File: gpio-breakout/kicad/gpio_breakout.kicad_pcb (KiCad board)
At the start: 2 copper layers, 63.5 x 30 mm, 12 parts, among them J1 FH41-40S-0.5SH(05), J2 Pi GPIO 2x20

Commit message: gpio-breakout: attach FH41 STEP model, tidy silk
Real connector model from the shared B2_INTERCONNECT.3dshapes now
renders on J1; redundant 3V3/GND silk texts removed (TP refs + README
cover them).

Co-Authored-By: Claude Fable 5 <noreply@anthropic.com>
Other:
- board text removed: "3V3"
- board text removed: "GND"
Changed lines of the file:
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@@
 		)
 		(embedded_fonts no)
-		(model "${KIPRJMOD}/B2_INTERCONNECT.3dshapes/FPC-SMD_FH41-40S-0.5SH.step"
+		(model "${KIPRJMOD}/../B2_INTERCONNECT.3dshapes/FPC-SMD_FH41-40S-0.5SH.step"
 			(offset
 				(xyz 0 0 0)
@@
 		(layer "F.SilkS")
 		(effects
-			(font
-				(size 1 1)
-				(thickness 0.15)
-			)
-		)
-	)
-	(gr_text "3V3"
-		(at 108.2 72.6 0)
-		(layer "F.SilkS")
-		(effects
-			(font
-				(size 1 1)
-				(thickness 0.15)
-			)
-		)
-	)
-	(gr_text "GND"
-		(at 108.2 78 0)
-		(layer "F.SilkS")
-		(effects

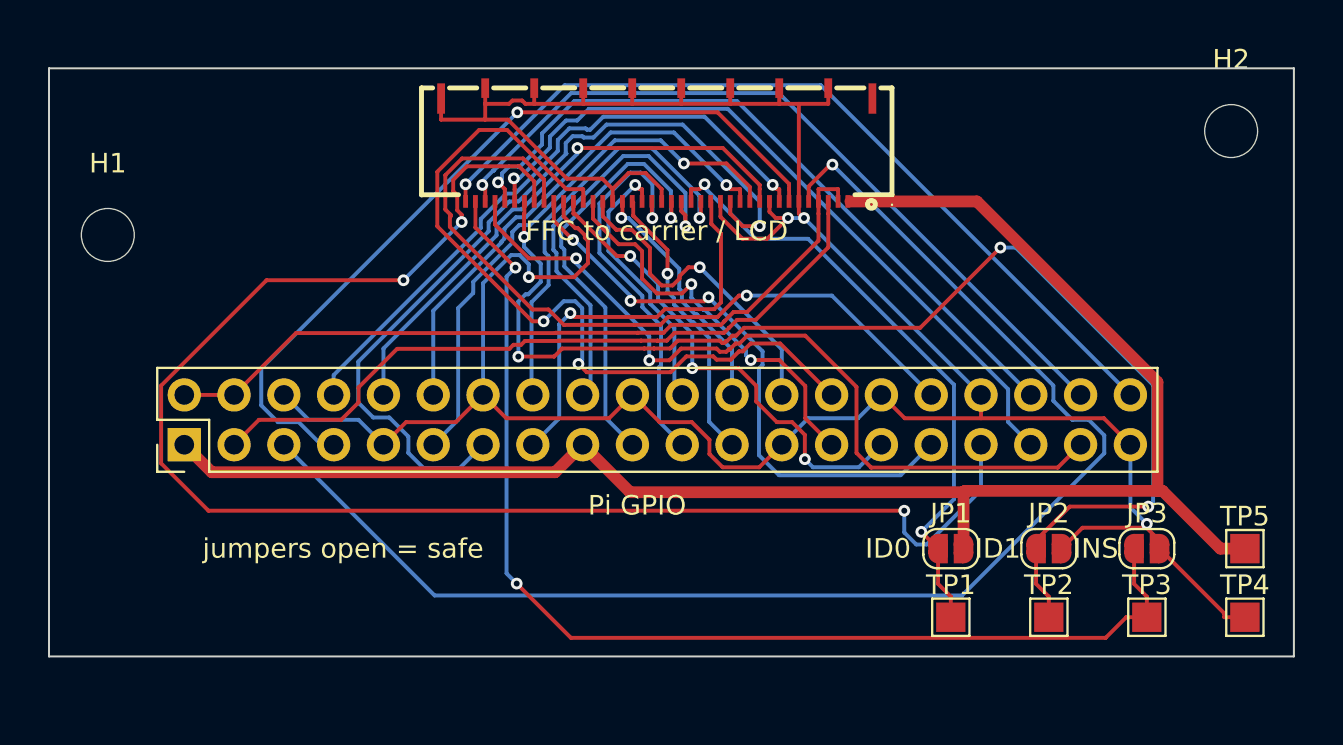
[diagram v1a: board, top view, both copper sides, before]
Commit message: gpio-breakout A1: address design review
4-layer with solid In1 GND plane + pours (review #2), corrected FH41
land pattern 0.30x0.65 with paste margin (#4), pads 41-50 shield to
GND (#4), fused + default-bridged/cuttable 5V/3V3 links (#3), symbol
pins retyped passive (#7), fresh all-severity ERC/DRC committed (#6,
#7), J2 assembly split defined (#9), honest gate statements in README
(#2, #8). Board grown to 63.5x32 for full routing: errors-only DRC
0/0/0, zero dangling copper. Fabrication remains gated on the
interconnect contract cable identity (#1, #5).

Co-Authored-By: Claude Fable 5 <noreply@anthropic.com>
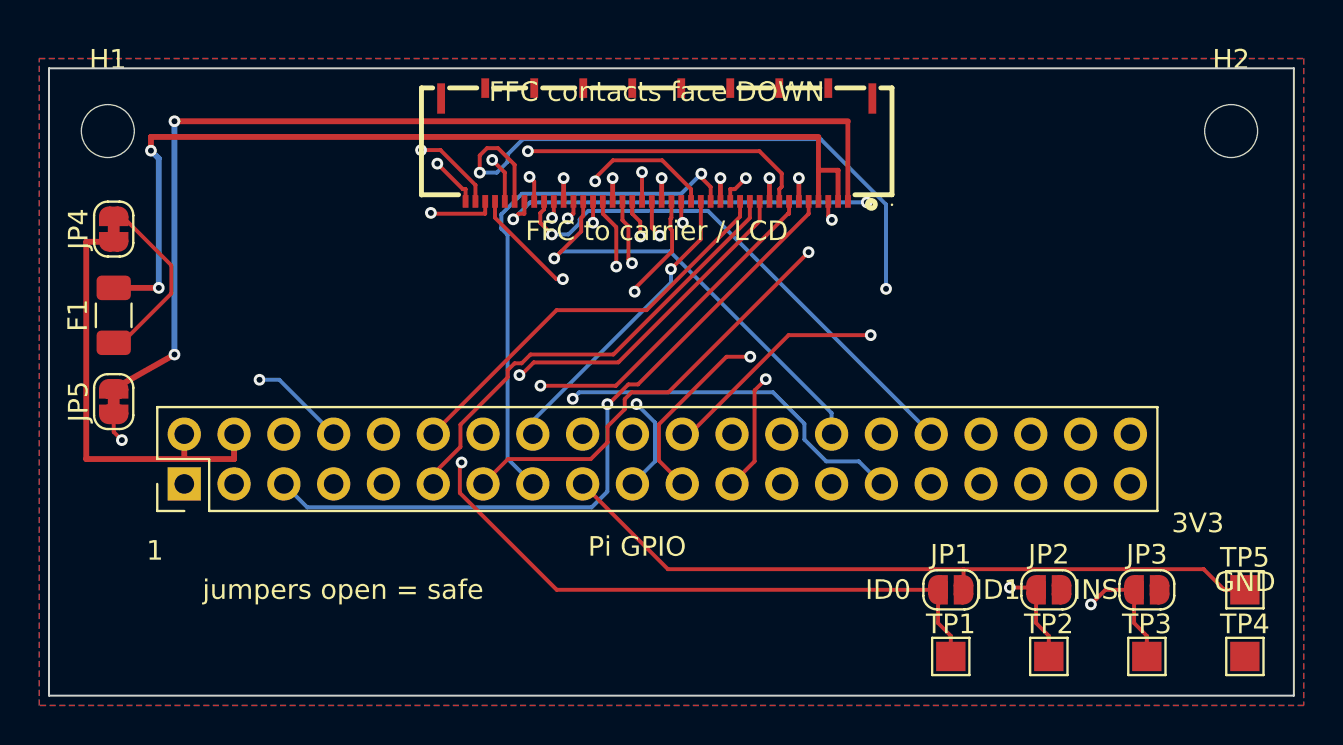
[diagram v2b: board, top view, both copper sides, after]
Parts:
- added F1: 0.5A polyfuse 1206, Fuse_1206_3216Metric, F.Cu at (53.3, 62.6)
- added JP4: 5V LINK, SolderJumper-2_P1.3mm_Bridged_RoundedPad1.0x1.5mm, F.Cu at (53.3, 58.2)
- added JP5: 3V3 LINK, SolderJumper-2_P1.3mm_Bridged_RoundedPad1.0x1.5mm, F.Cu at (53.3, 67.0)
- moved H1 5.30 mm to (53.0, 53.2)
- moved JP1 2.10 mm to (96.0, 76.6)
- moved JP2 2.10 mm to (101.0, 76.6)
- moved JP3 2.10 mm to (106.0, 76.6)
- moved TP5 2.10 mm to (111.0, 76.6)
- moved J2 2.00 mm to (56.9, 71.2)
- moved TP1 2.00 mm to (96.0, 80.0)
- moved TP2 2.00 mm to (101.0, 80.0)
- moved TP3 2.00 mm to (106.0, 80.0)
- moved TP4 2.00 mm to (111.0, 80.0)
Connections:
- J1 pad 1: +3V3 -> +3V3_FFC
- J1 pad 2: +5V -> +5V_FFC
- J1 pad 4: +5V -> +5V_FFC
- J1 pad 50: (no net) -> GND
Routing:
- net GND: track 152.0 -> 7.14 mm, vias 4 -> 6
- net +3V3_FFC: track 0.00 -> 53.9 mm, vias 0 -> 2
- net +5V_FFC: track 0.00 -> 50.1 mm, vias 0 -> 2
- net GPIO13: track 78.5 -> 36.3 mm, vias 3 -> 1
- net GPIO3: track 71.4 -> 36.7 mm
- net PANEL_ID0: track 31.7 -> 57.9 mm
- net +3V3: track 85.6 -> 64.2 mm, vias 0 -> 1
- net ID_SC: track 40.8 -> 22.3 mm, vias 2 -> 1
- net +5V: track 39.9 -> 22.6 mm
- net GPIO25: track 13.9 -> 31.1 mm, vias 1 -> 2
- net GPIO27: track 42.3 -> 29.0 mm, vias 1 -> 2
- net GPIO12: track 39.1 -> 26.7 mm
- net PANEL_ID1: track 63.5 -> 51.8 mm, vias 4 -> 3
- net GPIO4: track 41.2 -> 30.0 mm
- net +5V_LNK: track 0.00 -> 9.39 mm
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- added copper zone on B.Cu, net GND
- added copper zone on F.Cu, net GND
- added copper zone on In1.Cu, net GND
- added copper zone on In2.Cu, net GND
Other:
- board size 63.5 x 30 mm -> 63.5 x 32 mm
- copper layers 2 -> 4
- board text added: "1"
- board text added: "3V3"
- board text added: "FFC contacts face DOWN"
- board text added: "GND"
- board text added: "cut 5V/3V3 links if chain"
- board text added: "is externally powered"
- board text added: "koyomi gpio-breakout A1"
- board text removed: "koyomi gpio-breakout A0"
